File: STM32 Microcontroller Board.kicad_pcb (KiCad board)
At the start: 4 copper layers, 74.8 x 98.3 mm, 183 parts, among them J1 F407 SWD, J10 USB_B_Micro, J2 GPIO, J3 Conn_01x02_Pin, J4 F103 SWD, J5 USB_B_Micro, J6 Ethernet, J7 12V IN, J8 12V RGB LED, J9 Relay IO, Q1 PMOS, Q2 NMOS, Q3 NMOS, Q4 NMOS, SW1 SW_Push, SW2 SW_Push, SW3 SW_Push, SW4 SW_Push, SW5 SW_Push, SW6 SW_Push, U1 STM32F407VGTx, U2 MCP1825S-3302E/EB, U3 STM32F103C8T6, U4 USBLC6-2, U5 DP83826IRHBR, U6 TLV9001TIDCKR, U7 ULN2803CDWR, U8 USBLC6-2, Y1 8MHz, Y2 25MHz

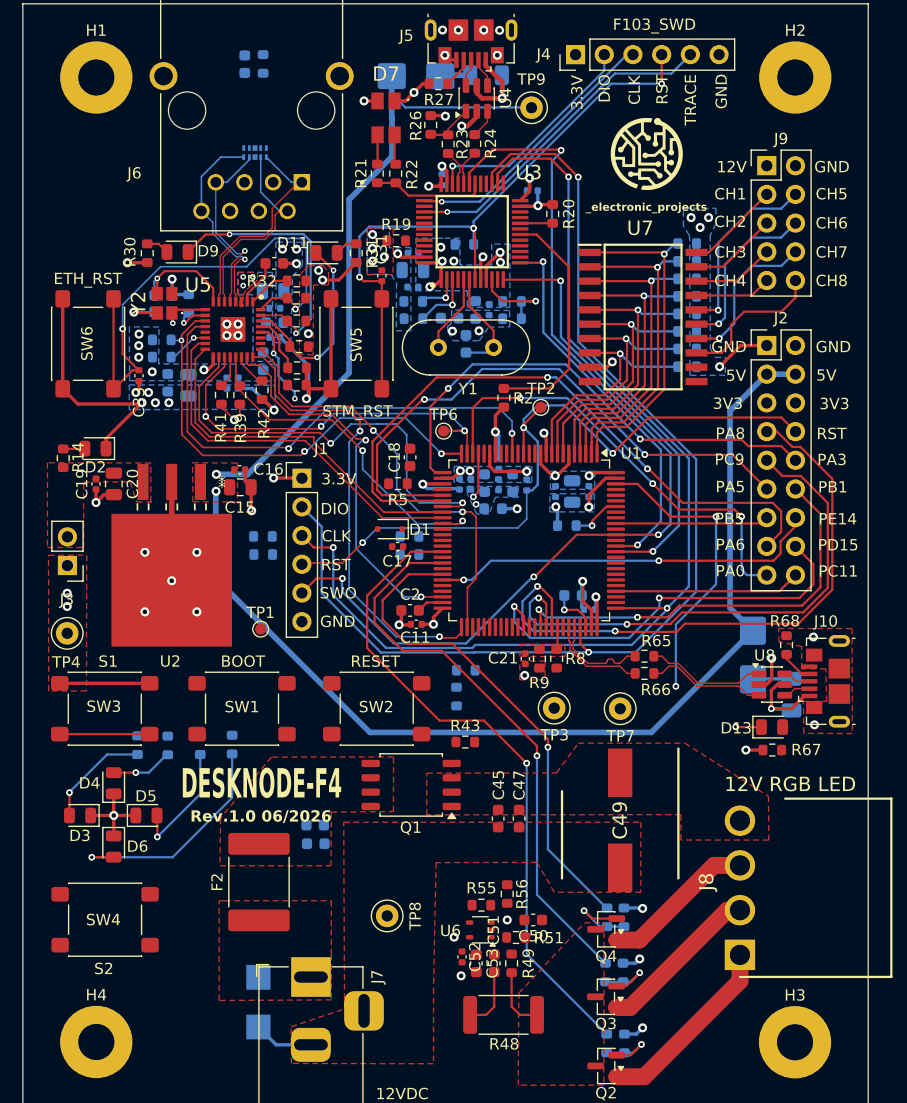
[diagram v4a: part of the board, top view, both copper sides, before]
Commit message: 12V i/p FIlter caps removed
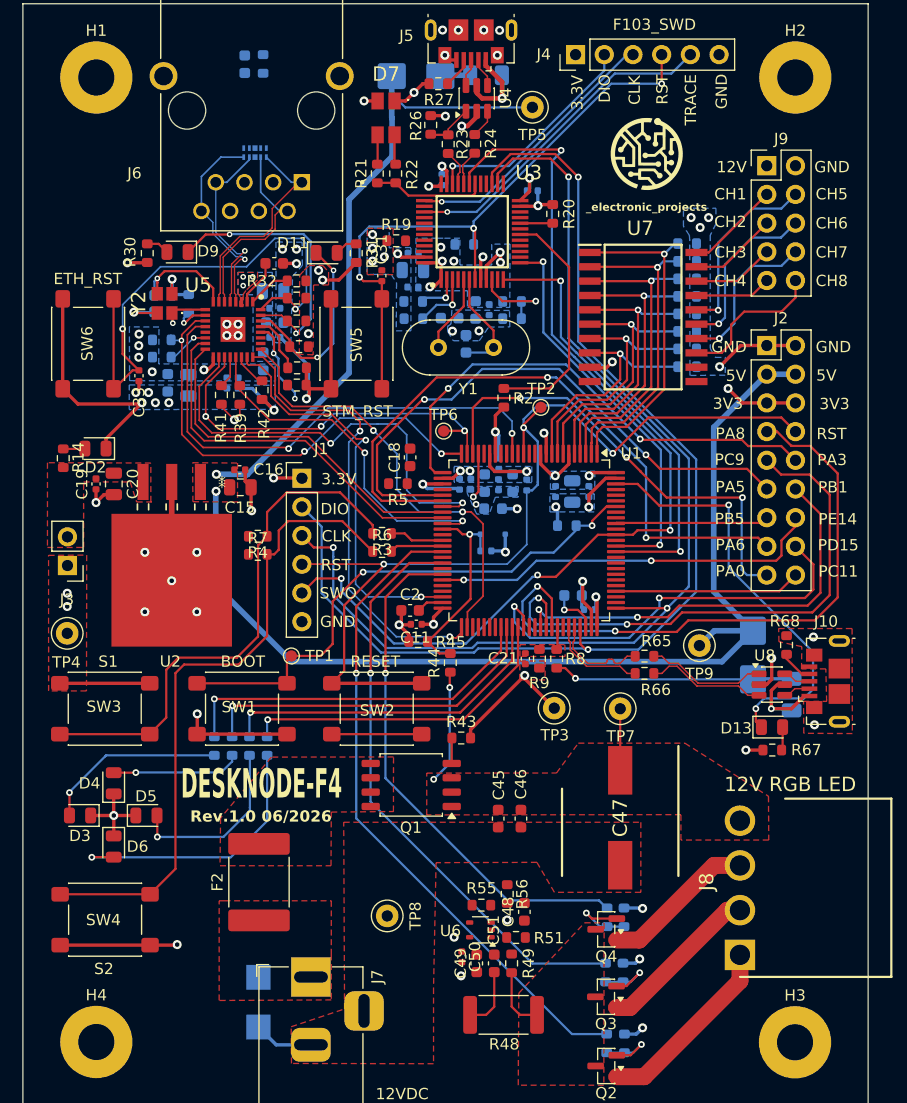
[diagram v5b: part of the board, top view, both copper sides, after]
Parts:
- removed C52: 0.1uF, Capacitor_SMD:C_0402_1005Metric
- removed C53: 1uF, Capacitor_SMD:C_0603_1608Metric
- added TP5: 5V, TestPoint:TestPoint_Keystone_5000-5004_Miniature, F.Cu at (146.2, 51.6)
- C17, D1: moved to B.Cu
- C46: value 1uF -> 0.1uF; moved to F.Cu
- C47: value 0.1uF -> 680uF; footprint Capacitor_SMD:C_0603_1608Metric -> footprints:UCL1E681MNL1GS
- C48: value 0.1uF -> 0.47uF; moved to F.Cu
- C49: value 680uF -> 0.47uF; footprint footprints:UCL1E681MNL1GS -> Capacitor_SMD:C_0603_1608Metric
- C50: value 0.47uF -> 0.1uF; footprint Capacitor_SMD:C_0603_1608Metric -> Capacitor_SMD:C_0402_1005Metric
- C51: value 0.47uF -> 1uF
- R3, R4, R44, R45, R6, R7: moved to F.Cu
- moved TP9 49.9 mm to (161.0, 99.2)
- moved C48 19.4 mm to (145.5, 122.8), turned to 90 degrees
- moved C46 18.2 mm to (145.2, 114.5), turned to -90 degrees
- moved C49 17.9 mm to (141.3, 127.3), turned to 90 degrees
- moved D1 9.10 mm to (142.7, 89.4), turned to 0 degrees
- moved C47 8.95 mm to (154.0, 114.5)
- moved C17 7.82 mm to (142.1, 90.8), turned to 0 degrees
- moved C50 7.12 mm to (140.0, 126.8), turned to -90 degrees
- moved R10 6.80 mm to (118.0, 108.1)
- moved R11 5.70 mm to (119.6, 108.1)
- moved R45 4.92 mm to (136.1, 98.9), turned to 180 degrees
- moved R12 4.36 mm to (121.2, 108.1)
- moved TP1 3.61 mm to (124.9, 100.1)
- moved R13 3.10 mm to (122.7, 108.1)
- moved R44 3.04 mm to (138.9, 100.7)
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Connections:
- C48 pad 1: +12V -> Net-(C48-Pad1)
- C49 pad 1: +12V -> GND
- C49 pad 2: GND -> Net-(U6-+)
- C50 pad 1: Net-(C50-Pad1) -> +3.3V
- C51 pad 1: GND -> +3.3V
- C51 pad 2: Net-(U6-+) -> GND
- R49 pad 2: Net-(C50-Pad1) -> Net-(C48-Pad1)
- R51 pad 1: Net-(C50-Pad1) -> Net-(C48-Pad1)
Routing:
- net Net-(R6-Pad2): track 0.00 -> 57.9 mm
- net /Main MCU/BOOT0: track 4.47 -> 47.4 mm, vias 1 -> 2
- net Net-(R3-Pad2): track 7.96 -> 47.0 mm
- net /Main MCU/PD11: track 0.00 -> 32.3 mm, vias 0 -> 1
- net /Main MCU/PD12: track 0.00 -> 31.1 mm, vias 0 -> 1
- net /Main MCU/PD13: track 0.00 -> 30.5 mm, vias 0 -> 1
- net /Main MCU/PD14: track 0.00 -> 29.1 mm, vias 0 -> 1
- net GND: track 148.5 -> 175.2 mm, vias 64 -> 65
- net +3.3V: track 66.1 -> 92.8 mm, vias 32 -> 35
- net /Main MCU/RESET: track 87.2 -> 109.0 mm
- net /Main MCU/PB1: track 0.00 -> 18.6 mm, vias 0 -> 1
- net /AC PWR ctrl & USB FS/USB_OTG_FS_VBUS: track 3.45 -> 21.2 mm, vias 0 -> 1
- net +12V: track 0.00 -> 15.5 mm, vias 0 -> 2
- net /AC PWR ctrl & USB FS/LED_USB_n: track 28.8 -> 37.9 mm, vias 3 -> 2
- net Net-(D3-A): track 9.48 -> 16.4 mm
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
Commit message: Updated layout
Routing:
- net +12V: track 15.5 -> 65.2 mm, vias 2 -> 4
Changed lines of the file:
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@@
 	)
 	(segment
-		(start 133.775 52.518596)
-		(end 133.775 55.925)
+		(start 118.175 93.8926)
+		(end 125.2824 101)
 		(width 0.5)
 		(layer "B.Cu")
@@
 	)
 	(segment
-		(start 162.9902 100.6348)
+		(start 162.625 101)
 		(end 165.725 97.9)
 		(width 0.5)
@@
 	)
 	(segment
+		(start 133.775 52.518596)
+		(end 133.775 55.925)
+		(width 0.5)
+		(layer "B.Cu")
+		(net 7)
+	)
+	(segment
 		(start 120.8758 84.0508)
 		(end 118.225 84.0508)
@@
 	)
 	(segment
-		(start 118.175 93.8926)
-		(end 124.9172 100.6348)
+		(start 125.2824 101)
+		(end 162.625 101)
 		(width 0.5)
 		(layer "B.Cu")
@@
 	)
 	(segment
-		(start 124.9172 100.6348)
-		(end 162.9902 100.6348)
+		(start 133.775 55.925)
+		(end 129.975 59.725)
 		(width 0.5)
 		(layer "B.Cu")
@@
 	)
 	(segment
-		(start 133.775 55.925)
-		(end 129.975 59.725)
+		(start 118.2 85.5508)
+		(end 118.175 85.5758)
 		(width 0.5)
 		(layer "B.Cu")
@@
 	)
 	(segment
-		(start 118.2 85.5508)
-		(end 118.175 85.5758)
-		(width 0.5)
-		(layer "B.Cu")
-		(net 7)
-	)
-	(segment
 		(start 162.2552 94.4302)
 		(end 165.725 97.9)
@@
 	)
 	(segment
+		(start 151.7 102.550809)
+		(end 151.7 107.9776)
+		(width 0.3)
+		(layer "F.Cu")
+		(net 20)
+	)
+	(segment
 		(start 138.8872 102.9208)
 		(end 138.8872 101.6122)
@@
 	)
 	(segment
+		(start 160.725 74.57)
+		(end 159.93 74.57)
+		(width 0.3)
+		(layer "F.Cu")
+		(net 20)
+	)
+	(segment
 		(start 153.9748 104.8004)
 		(end 153.9748 110.2524)
-		(width 0.2)
+		(width 0.3)
+		(layer "F.Cu")
+		(net 20)
+	)
+	(segment
+		(start 149.449192 100.3)
+		(end 149.4744 100.3)
+		(width 0.3)
 		(layer "F.Cu")
 		(net 20)
@@
 		(net 20)
 	)
+	(segment
+		(start 149.399192 100.250001)
+		(end 151.7 102.550809)
+		(width 0.3)
+		(layer "F.Cu")
+		(net 20)
+	)
+	(segment
+		(start 159.93 74.57)
+		(end 158.7 75.8)
+		(width 0.3)
+		(layer "F.Cu")
+		(net 20)
+	)
+	(segment
+		(start 151.7 107.9776)
+		(end 153.9748 110.2524)
+		(width 0.3)
+		(layer "F.Cu")
+		(net 20)
+	)
+	(segment
+		(start 149.399192 100.250001)
+		(end 149.449192 100.3)
+		(width 0.3)
+		(layer "F.Cu")
+		(net 20)
+	)
+	(via
+		(at 149.399192 100.250001)
+		(size 0.6)
+		(drill 0.3)
+		(layers "F.Cu" "B.Cu")
+		(net 20)
+	)
 	(via
 		(at 138.8872 102.9208)
@@
 	)
 	(via
+		(at 158.7 75.8)
+		(size 0.6)
+		(drill 0.3)
+		(layers "F.Cu" "B.Cu")
+		(net 20)
+	)
+	(via
 		(at 137.4648 111.0488)
 		(size 0.6)
@@
 	)
 	(segment
+		(start 157.2278 100.2222)
+		(end 161.45 96)
+		(width 0.3)
+		(layer "B.Cu")
+		(net 20)
+	)
+	(segment
+		(start 149.399192 100.250001)
+		(end 149.426993 100.2222)
+		(width 0.3)
+		(layer "B.Cu")
+		(net 20)
+	)
+	(segment
+		(start 161.45 96)
+		(end 161.45 78.55)
+		(width 0.3)
+		(layer "B.Cu")
+		(net 20)
+	)
+	(segment
+		(start 161.45 78.55)
+		(end 158.7 75.8)
+		(width 0.3)
+		(layer "B.Cu")
+		(net 20)
+	)
+	(segment
 		(start 137.4648 111.0488)
 		(end 138.8872 109.6264)
@@
 	)
 	(segment
+		(start 149.426993 100.2222)
+		(end 157.2278 100.2222)
+		(width 0.3)
+		(layer "B.Cu")
+		(net 20)
+	)
+	(segment
 		(start 104.675 81.8008)
 		(end 106.5625 81.8008)
@@
 	)
 	(segment
-		(start 144.2715 55.701)
-		(end 142.625 57.3475)
+		(start 150.9334 99.5584)
+		(end 150.450405 99.075405)
 		(width 0.2)
 		(layer "F.Cu")
@@
 	)
 	(segment
-		(start 150.450405 97.600405)
-		(end 150.425 97.575)
+		(start 144.2715 55.701)
+		(end 142.625 57.3475)
 		(width 0.2)
 		(layer "F.Cu")
@@
 	)
 	(segment
-		(start 148.226 55.701)
-		(end 144.2715 55.701)
+		(start 150.450405 97.600405)
+		(end 150.425 97.575)
 		(width 0.2)
 		(layer "F.Cu")
@@
 	)
 	(segment
-		(start 142.625 57.3475)
-		(end 142.625 58.337)
+		(start 148.226 55.701)
+		(end 144.2715 55.701)
 		(width 0.2)
 		(layer "F.Cu")
@@
 	)
 	(segment
-		(start 150.2625 57.7375)
-		(end 148.226 55.701)
+		(start 151.13 99.5584)
+		(end 150.9334 99.5584)
 		(width 0.2)
 		(layer "F.Cu")
@@
 	)
 	(segment
-		(start 151.13 99.5584)
-		(end 150.9334 99.5584)
+		(start 142.625 57.3475)
+		(end 142.625 58.337)
 		(width 0.2)
 		(layer "F.Cu")
@@
 	)
 	(segment
-		(start 150.9334 99.5584)
-		(end 150.450405 99.075405)
+		(start 150.2625 57.7375)
+		(end 148.226 55.701)
 		(width 0.2)
 		(layer "F.Cu")
@@
 	)
 	(segment
-		(start 151.3332 99.568)
-		(end 155.582 99.568)
+		(start 141.400643 99.4664)
+		(end 141.042043 99.825)
 		(width 0.2)
 		(layer "B.Cu")
@@
 	)
 	(segment
-		(start 151.13 99.7712)
-		(end 151.3332 99.568)
+		(start 132.8 99.825)
+		(end 127.55 94.575)
 		(width 0.2)
 		(layer "B.Cu")
@@
 	)
 	(segment
-		(start 150.7332 99.4664)
-		(end 141.400643 99.4664)
+		(start 160.7 82.725)
+		(end 150.2625 72.2875)
 		(width 0.2)
 		(layer "B.Cu")
@@
 	)
 	(segment
-		(start 127.55 88.685)
-		(end 125.8 86.935)
+		(start 141.042043 99.825)
+		(end 132.8 99.825)
 		(width 0.2)
 		(layer "B.Cu")
@@
 	)
 	(segment
-		(start 141.042043 99.825)
-		(end 132.8 99.825)
+		(start 150.8252 99.5584)
+		(end 150.7332 99.4664)
 		(width 0.2)
 		(layer "B.Cu")
@@
 	)
 	(segment
-		(start 127.55 94.575)
-		(end 127.55 88.685)
+		(start 127.55 88.685)
+		(end 125.8 86.935)
 		(width 0.2)
 		(layer "B.Cu")
@@
 	)
 	(segment
-		(start 160.7 82.725)
-		(end 150.2625 72.2875)
+		(start 151.13 99.7712)
+		(end 151.3332 99.568)
 		(width 0.2)
 		(layer "B.Cu")
@@
 	)
 	(segment
-		(start 150.8252 99.5584)
-		(end 150.7332 99.4664)
+		(start 151.13 99.5584)
+		(end 150.8252 99.5584)
 		(width 0.2)
 		(layer "B.Cu")
@@
 	)
 	(segment
-		(start 150.2625 72.2875)
-		(end 150.2625 57.7375)
+		(start 151.3332 99.568)
+		(end 155.582 99.568)
 		(width 0.2)
 		(layer "B.Cu")
@@
 	)
 	(segment
-		(start 155.582 99.568)
-		(end 160.7 94.45)
+		(start 150.7332 99.4664)
+		(end 141.400643 99.4664)
 		(width 0.2)
 		(layer "B.Cu")
@@
 	)
 	(segment
-		(start 132.8 99.825)
-		(end 127.55 94.575)
+		(start 151.13 99.5584)
+		(end 151.13 99.7712)
 		(width 0.2)
 		(layer "B.Cu")
@@
 	)
 	(segment
-		(start 141.400643 99.4664)
-		(end 141.042043 99.825)
+		(start 160.7 94.45)
+		(end 160.7 82.725)
 		(width 0.2)
 		(layer "B.Cu")
@@
 	)
 	(segment
-		(start 151.13 99.5584)
-		(end 151.13 99.7712)
+		(start 155.582 99.568)
+		(end 160.7 94.45)
 		(width 0.2)
 		(layer "B.Cu")
@@
 	)
 	(segment
-		(start 160.7 94.45)
-		(end 160.7 82.725)
+		(start 150.2625 72.2875)
+		(end 150.2625 57.7375)
 		(width 0.2)
 		(layer "B.Cu")
@@
 	)
 	(segment
-		(start 151.13 99.5584)
-		(end 150.8252 99.5584)
+		(start 127.55 94.575)
+		(end 127.55 88.685)
 		(width 0.2)
 		(layer "B.Cu")
@@
 	)
 	(via
-		(at 130.6068 101.6508)
+		(at 130.6092 101.8)
 		(size 0.6)
 		(drill 0.3)
@@
 	)
 	(via
-		(at 131.8768 101.6508)
+		(at 131.8792 101.8)
 		(size 0.6)
 		(drill 0.3)
@@
 	)
 	(via
-		(at 133.1976 101.6508)
+		(at 133.2 101.8)
 		(size 0.6)
 		(drill 0.3)

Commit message: Layout complete with DRC resolution
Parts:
- moved R29 14.4 mm to (110.2, 55.4)
- moved C32 14.4 mm to (108.6, 55.4)
- moved C48 5.32 mm to (142.8, 127.4), turned to -90 degrees
- moved C49 4.32 mm to (144.4, 124.3), turned to -90 degrees
- moved TP1 2.68 mm to (127.5, 100.2)
- moved C51 2.60 mm to (140.2, 127.4), turned to -90 degrees
- moved F2 1.80 mm to (123.5, 121.1)
- moved C50 1.67 mm to (141.5, 127.4)
- moved R51 1.38 mm to (145.9, 125.8), turned to 90 degrees
- moved R56 1.34 mm to (145.0, 122.0), turned to 180 degrees
- moved D6 1.03 mm to (108.4, 117.7)
- moved SW4 1.03 mm to (108.3, 124.5)
- moved G*** 0.92 mm to (155.4, 55.9)
- moved D3 0.92 mm to (105.4, 114.8)
- moved D4 0.92 mm to (108.4, 111.9)
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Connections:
- H1 pad 1: (no net) -> Earth
- H2 pad 1: (no net) -> Earth
- H3 pad 1: (no net) -> Earth
- H4 pad 1: (no net) -> Earth
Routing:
- net /LED Driver/I_sense: track 0.00 -> 73.8 mm, vias 0 -> 4
- net GND: track 175.2 -> 200.2 mm, vias 65 -> 71
- net +12V: track 65.2 -> 90.0 mm
- net Earth: track 0.00 -> 12.0 mm
- net +3.3V: track 92.8 -> 99.2 mm
- net /Main MCU/PA4: track 0.00 -> 4.90 mm
- net Net-(D12-A2): track 0.00 -> 4.66 mm
- net Net-(U6--): track 0.00 -> 3.34 mm
- net Net-(U6-+): track 0.00 -> 3.23 mm
- net Net-(C48-Pad1): track 0.00 -> 3.15 mm
- net /LED Driver/G_PWM: track 52.2 -> 49.1 mm
- net Net-(U3-PD0-OSC_IN): track 7.28 -> 9.97 mm
- net /Main MCU/RESET: track 109.0 -> 111.5 mm
- net /Ethernet PHY/RD_N: track 18.1 -> 20.4 mm
- net /LED Driver/B_PWM: track 46.3 -> 44.2 mm
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- added copper zone on B.Cu, net Earth
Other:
- board text added: "12V RGB LED"
- board text added: "ERR"
- board text added: "PWR"
- board text added: "STAT"
- board text added: "USR"

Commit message: Review files
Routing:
- net +3.3V: vias 35 -> 36
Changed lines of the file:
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@@
+	)
+	(via
+		(at 106.15 94.575)
+		(size 0.8)
+		(drill 0.4)
+		(layers "F.Cu" "B.Cu")
+		(free yes)
+		(net 6)
 	)
 	(via
@@
 	)
 	(via
-		(at 105.025 95.7508)
+		(at 103.95 94.575)
 		(size 0.8)
 		(drill 0.4)
@@
 	)
 	(via
-		(at 105.025 94.5758)
+		(at 105.05 94.575)
 		(size 0.8)
 		(drill 0.4)
